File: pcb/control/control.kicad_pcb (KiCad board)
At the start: 2 copper layers, 100 x 80 mm, 30 parts, among them J1 Barrel_Jack_MountingPin, J2 Screw_Terminal_01x02, SW1 OS102011MS2QN1, SW2 OS102011MS2QN1, U1 PicoW, U2 SN65HVD230DR, U3 FDN340P, U4 DMG2305UX-7

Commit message: Control PCB done
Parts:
- added D10: LED, LED_THT:LED_D5.0mm, F.Cu at (159.5, 126.0)
- added D6: LED, LED_THT:LED_D5.0mm, F.Cu at (152.5, 112.0)
- added D7: LED, LED_THT:LED_D5.0mm, F.Cu at (152.5, 119.0)
- added D8: LED, LED_THT:LED_D5.0mm, F.Cu at (159.5, 119.0)
- added D9: LED, LED_THT:LED_D5.0mm, F.Cu at (152.5, 126.0)
- added G***: LOGO, LOGO, F.Cu at (186.5, 131.0)
- added R13: 60Ω, Resistor_SMD:R_1206_3216Metric, F.Cu at (147.5, 111.7)
- added R14: 60Ω, Resistor_SMD:R_1206_3216Metric, F.Cu at (147.5, 118.7)
- added R15: 60Ω, Resistor_SMD:R_1206_3216Metric, F.Cu at (164.5, 118.7)
- added R16: 60Ω, Resistor_SMD:R_1206_3216Metric, F.Cu at (147.5, 125.7)
- added R17: 60Ω, Resistor_SMD:R_1206_3216Metric, F.Cu at (164.5, 125.7)
- J2: value Screw_Terminal_01x02 -> 1729092; footprint TerminalBlock_TE-Connectivity:TerminalBlock_TE_282834-2_1x02_P2.54mm_Horizontal -> 1729092:PHOENIX_1729092
- moved U4 94.0 mm to (188.5, 60.5), turned to -90 degrees
- moved R12 66.6 mm to (139.5, 65.0), turned to 90 degrees
- moved J1 63.9 mm to (190.0, 67.7), turned to 90 degrees
- moved R10 63.2 mm to (116.5, 64.5), turned to 90 degrees
- moved CR1 62.2 mm to (188.6, 121.0), turned to 180 degrees
- moved D3 61.5 mm to (111.3, 64.8), turned to 90 degrees
- moved U2 60.9 mm to (174.7, 120.9)
- moved R1 56.1 mm to (181.1, 119.5)
- moved R2 55.8 mm to (181.1, 122.5), turned to 180 degrees
- moved D4 53.4 mm to (122.7, 64.8), turned to 90 degrees
- moved R11 52.9 mm to (128.0, 64.5), turned to 90 degrees
- moved D5 47.8 mm to (134.1, 64.8), turned to 90 degrees
- moved SW1 38.7 mm to (149.5, 70.6)
- moved SW2 34.7 mm to (149.5, 81.6)
- moved R4 32.9 mm to (188.4, 112.0), turned to -90 degrees
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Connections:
- CR1 pad 1: /CANH -> /CANL
- CR1 pad 2: /CANL -> /CANH
- U1 pad 24: unconnected-(U1-GPIO18-Pad24)_1 -> /WFACE
- U1 pad 25: unconnected-(U1-GPIO19-Pad25) -> /EFACE
- U1 pad 26: unconnected-(U1-GPIO20-Pad26) -> /SFACE
- U1 pad 27: unconnected-(U1-GPIO21-Pad27)_1 -> /NFACE
- U1 pad 31: /POT_R -> /POT_B
- U1 pad 34: /POT_B -> /POT_R
- U1 pad 5: unconnected-(U1-GPIO3-Pad5)_1 -> /SENSORS
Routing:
- net VSYS: track 0.00 -> 259.8 mm, vias 0 -> 3
- net GND: track 0.00 -> 125.0 mm, vias 0 -> 15
- net /POT_R: track 0.00 -> 107.1 mm
- net /POT_G: track 0.00 -> 94.7 mm
- net /CANL: track 0.00 -> 88.3 mm
- net /POT_B: track 0.00 -> 86.1 mm
- net /LED_R: track 0.00 -> 83.4 mm, vias 0 -> 1
- net /CANH: track 0.00 -> 80.3 mm
- net /LED_G: track 0.00 -> 72.6 mm, vias 0 -> 1
- net /LED_B: track 0.00 -> 62.8 mm
- net /SENSORS: track 0.00 -> 55.4 mm
- net /SFACE: track 0.00 -> 43.9 mm
- net /NFACE: track 0.00 -> 41.4 mm
- net /WFACE: track 0.00 -> 34.5 mm, vias 0 -> 1
- net /EFACE: track 0.00 -> 31.6 mm
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- added copper zone on F.Cu, net /CAN_ENL
- added copper zone on F.Cu, net /CAN_RS
- added copper zone on F.Cu, net /CAN_VREF
- added copper zone on B.Cu, net GND
- added copper zone on F.Cu, net GND
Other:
- board size 100 x 80 mm -> 95 x 80.5 mm
- board text added: "5V Supply"
- board text added: "ACM '24 '25"
- board text added: "BLUE"
- board text added: "CAN"
- board text added: "EAST"
- board text added: "GREEN"
- board text added: "H"
- board text added: "L"
- board text added: "LED Control Panel"
- board text added: "LIGHT"
- board text added: "MODE"
- board text added: "MUSIC"
- board text added: "NORTH"
- board text added: "OFF"
- board text added: "ON"
- board text added: "RED"
- board text added: "SENSORS"
- board text added: "SOUTH"
- board text added: "SYSTEM"
- board text added: "WEST"
- board text added: "WiFi"

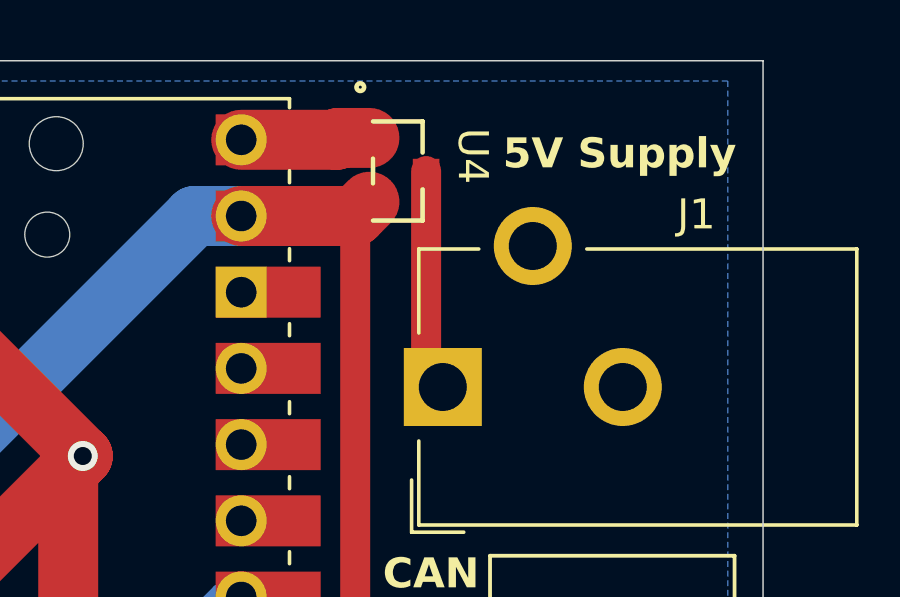
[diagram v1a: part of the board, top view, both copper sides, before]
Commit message: Increase power trace width
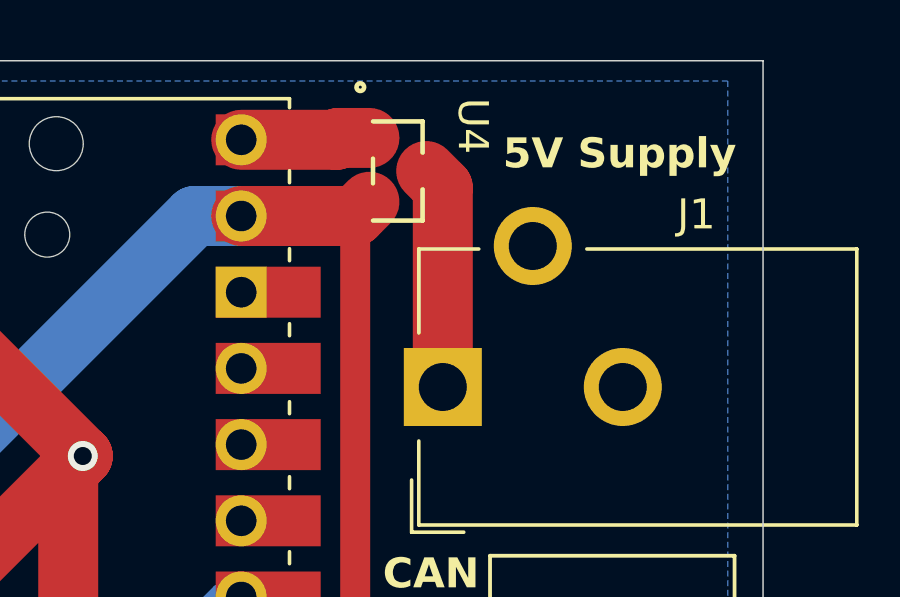
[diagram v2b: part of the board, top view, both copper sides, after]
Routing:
- net VBARREL: track 7.43 -> 8.21 mm
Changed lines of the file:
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@@
 		(tags "DMG2305UX-7 ")
 		(property "Reference" "U4"
-			(at -0.5 -2.5 -90)
+			(at -1.5 -2.5 -90)
 			(unlocked yes)
 			(layer "F.SilkS")
@@
 	(segment
 		(start 189.445 60.5)
-		(end 189.445 67.145)
-		(width 1)
+		(end 190 61.055)
+		(width 2)
+		(layer "F.Cu")
+		(net 16)
+	)
+	(segment
+		(start 190 61.055)
+		(end 190 67.7)
+		(width 2)
 		(layer "F.Cu")
 		(net 16)

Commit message: PCBs hopefully done
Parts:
- added H1: MountingHole, MountingHole:MountingHole_3.2mm_M3_DIN965_Pad, F.Cu at (100.5, 61.0)
- added H2: MountingHole, MountingHole:MountingHole_3.2mm_M3_DIN965_Pad, F.Cu at (100.5, 106.0)
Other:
- board size 95 x 80.5 mm -> 104.5 x 80 mm
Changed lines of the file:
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@@
 		)
 	)
+	(footprint "MountingHole:MountingHole_3.2mm_M3_DIN965_Pad"
+		(layer "F.Cu")
+		(at 100.5 61)
+		(descr "Mounting Hole 3.2mm, M3, DIN965")
+		(tags "mounting hole 3.2mm m3 din965")
+		(property "Reference" "H1"
+			(at 0 4.5 0)
+			(layer "F.SilkS")
+			(effects
+				(font
+					(size 1 1)
+					(thickness 0.15)
+				)
+			)
+		)
+		(property "Value" "MountingHole"
+			(at 0 3.8 0)
+			(layer "F.Fab")
+			(hide yes)
+			(effects
+				(font
+					(size 1 1)
+					(thickness 0.15)
+				)
+			)
+		)
+		(property "Footprint" "MountingHole:MountingHole_3.2mm_M3_DIN965_Pad"
+			(at 0 0 0)
+			(unlocked yes)
+			(layer "F.Fab")
+			(hide yes)
+			(effects
+				(font
+					(size 1.27 1.27)
+					(thickness 0.15)
+				)
+			)
+		)
+		(property "Datasheet" ""
+			(at 0 0 0)
+			(unlocked yes)
+			(layer "F.Fab")
+			(hide yes)
+			(effects
+				(font
+					(size 1.27 1.27)
+					(thickness 0.15)
+				)
+			)
+		)
+		(property "Description" "Mounting Hole without connection"
+			(at 0 0 0)
+			(unlocked yes)
+			(layer "F.Fab")
+			(hide yes)
+			(effects
+				(font
+					(size 1.27 1.27)
+					(thickness 0.15)
+				)
+			)
+		)
+		(property ki_fp_filters "MountingHole*")
+		(sheetname "Root")
+		(sheetfile "control.kicad_sch")
+		(attr exclude_from_pos_files exclude_from_bom)
+		(fp_circle
+			(center 0 0)
+			(end 2.8 0)
+			(stroke
+				(width 0.15)
+				(type solid)
+			)
+			(fill none)
+			(layer "Cmts.User")
+		)
+		(fp_circle
+			(center 0 0)
+			(end 3.05 0)
+			(stroke
+				(width 0.05)
+				(type solid)
+			)
+			(fill none)
+			(layer "F.CrtYd")
+		)
+		(fp_text user "${REFERENCE}"
+			(at 0 0 0)
+			(layer "F.Fab")
+			(effects
+				(font
+					(size 1 1)
+					(thickness 0.15)
+				)
+			)
+		)
+		(pad "1" thru_hole circle
+			(at 0 0)
+			(size 5.6 5.6)
+			(drill 3.2)
+			(layers "*.Cu" "*.Mask")
+			(remove_unused_layers no)
+		)
+	)
 	(footprint "LED_THT:LED_D5.0mm"
 		(layer "F.Cu")
@@
 		)
 	)
+	(footprint "MountingHole:MountingHole_3.2mm_M3_DIN965_Pad"
+		(layer "F.Cu")
+		(at 100.5 106)
+		(descr "Mounting Hole 3.2mm, M3, DIN965")
+		(tags "mounting hole 3.2mm m3 din965")
+		(property "Reference" "H2"
+			(at 0 -3.8 0)
+			(layer "F.SilkS")
+			(effects
+				(font
+					(size 1 1)
+					(thickness 0.15)
+				)
+			)
+		)
+		(property "Value" "MountingHole"
+			(at 0 3.8 0)
+			(layer "F.Fab")
+			(hide yes)
+			(effects
+				(font
+					(size 1 1)
+					(thickness 0.15)
+				)
+			)
+		)
+		(property "Footprint" "MountingHole:MountingHole_3.2mm_M3_DIN965_Pad"
+			(at 0 0 0)
+			(unlocked yes)
+			(layer "F.Fab")
+			(hide yes)
+			(effects
+				(font
+					(size 1.27 1.27)
+					(thickness 0.15)
+				)
+			)
+		)
+		(property "Datasheet" ""
+			(at 0 0 0)
+			(unlocked yes)
+			(layer "F.Fab")
+			(hide yes)
+			(effects
+				(font
+					(size 1.27 1.27)
+					(thickness 0.15)
+				)
+			)
+		)
+		(property "Description" "Mounting Hole without connection"
+			(at 0 0 0)
+			(unlocked yes)
+			(layer "F.Fab")
+			(hide yes)
+			(effects
+				(font
+					(size 1.27 1.27)
+					(thickness 0.15)
+				)
+			)
+		)
+		(property ki_fp_filters "MountingHole*")
+		(sheetname "Root")
+		(sheetfile "control.kicad_sch")
+		(attr exclude_from_pos_files exclude_from_bom)
+		(fp_circle
+			(center 0 0)
+			(end 2.8 0)
+			(stroke
+				(width 0.15)
+				(type solid)
+			)
+			(fill none)
+			(layer "Cmts.User")
+		)
+		(fp_circle
+			(center 0 0)
+			(end 3.05 0)
+			(stroke
+				(width 0.05)
+				(type solid)
+			)
+			(fill none)
+			(layer "F.CrtYd")
+		)
+		(fp_text user "${REFERENCE}"
+			(at 0 0 0)
+			(layer "F.Fab")
+			(effects
+				(font
+					(size 1 1)
+					(thickness 0.15)
+				)
+			)
+		)
+		(pad "1" thru_hole circle
+			(at 0 0)
+			(size 5.6 5.6)
+			(drill 3.2)
+			(layers "*.Cu" "*.Mask")
+			(remove_unused_layers no)
+		)
+	)
 	(footprint "Capacitor_SMD:C_0603_1608Metric"
 		(layer "F.Cu")
@@
 	)
 	(gr_rect
-		(start 105.675 56.825)
+		(start 96.175 57.325)
 		(end 200.675 137.325)
 		(stroke

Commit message: Final boards
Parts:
- D1, D10, D2, D3, D4, D5, D6, D7, D8, D9: footprint LED_THT:LED_D5.0mm -> LED_SMD:LED_0603_1608Metric
- R10, R13, R14, R15, R16, R17, R8, R9: value 60Ω -> 750Ω
- R11: value 60Ω -> 325Ω; footprint Resistor_SMD:R_1206_3216Metric -> Resistor_SMD:R_0603_1608Metric
- R12: value 5Ω -> 325Ω
- moved D10 1.62 mm to (160.0, 124.5)
- moved D8 1.58 mm to (160.0, 117.5)
- moved D9 1.54 mm to (152.5, 124.5)
- moved D6 1.50 mm to (152.5, 110.5)
- moved D1 1.27 mm to (157.0, 71.0)
- moved D7 1.21 mm to (152.5, 117.8)
- moved D3 1.01 mm to (111.5, 63.8)
- moved D2 0.98 mm to (157.0, 82.3)
- moved D4 0.83 mm to (123.0, 64.0)
- moved D5 0.78 mm to (134.0, 64.0)
- moved R11 0.21 mm to (128.0, 64.3)
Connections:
- C2 pad 1: VSYS -> +3V3
- C3 pad 1: VSYS -> +3V3
- R4 pad 1: VSYS -> +3V3
- R5 pad 1: VSYS -> +3V3
- R6 pad 1: VSYS -> +3V3
- R7 pad 1: VSYS -> +3V3
- S1 pad 8: VSYS -> +3V3
- SW1 pad 1: VSYS -> +3V3
- SW2 pad 1: VSYS -> +3V3
- U1 pad 36: unconnected-(U1-3V3-Pad36) -> +3V3
- U2 pad 3: VSYS -> +3V3
- U3 pad 2: VSYS -> +3V3
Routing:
- net VSYS: track 259.8 -> 4.47 mm, vias 3 -> 0
- net +3V3: track 0.00 -> 243.5 mm, vias 0 -> 3
- net /LED_B: track 62.8 -> 63.8 mm, vias 0 -> 1
- net Net-(D4-K): track 5.81 -> 5.16 mm
- net /NFACE: track 41.4 -> 41.9 mm
- net /SENSORS: track 55.4 -> 55.8 mm, vias 0 -> 1
- net /WFACE: vias 1 -> 2
